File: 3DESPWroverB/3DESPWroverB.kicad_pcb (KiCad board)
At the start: 2 copper layers, 40 x 40 mm, 18 parts, among them J1 Conn_02x07_Odd_Even, J10 Conn_02x03_Odd_Even, J11 Conn_01x01, J12 Conn_01x01, J13 Conn_01x01, J14 Conn_01x01, J15 Conn_01x01, J16 Conn_01x01, J17 Conn_01x01, J18 Conn_01x01, J2 Conn_01x01, J3 Conn_01x01, J4 Conn_01x01, J5 Conn_01x01, J6 Conn_01x01, J7 Conn_01x01, J8 Conn_01x01, J9 Conn_01x01

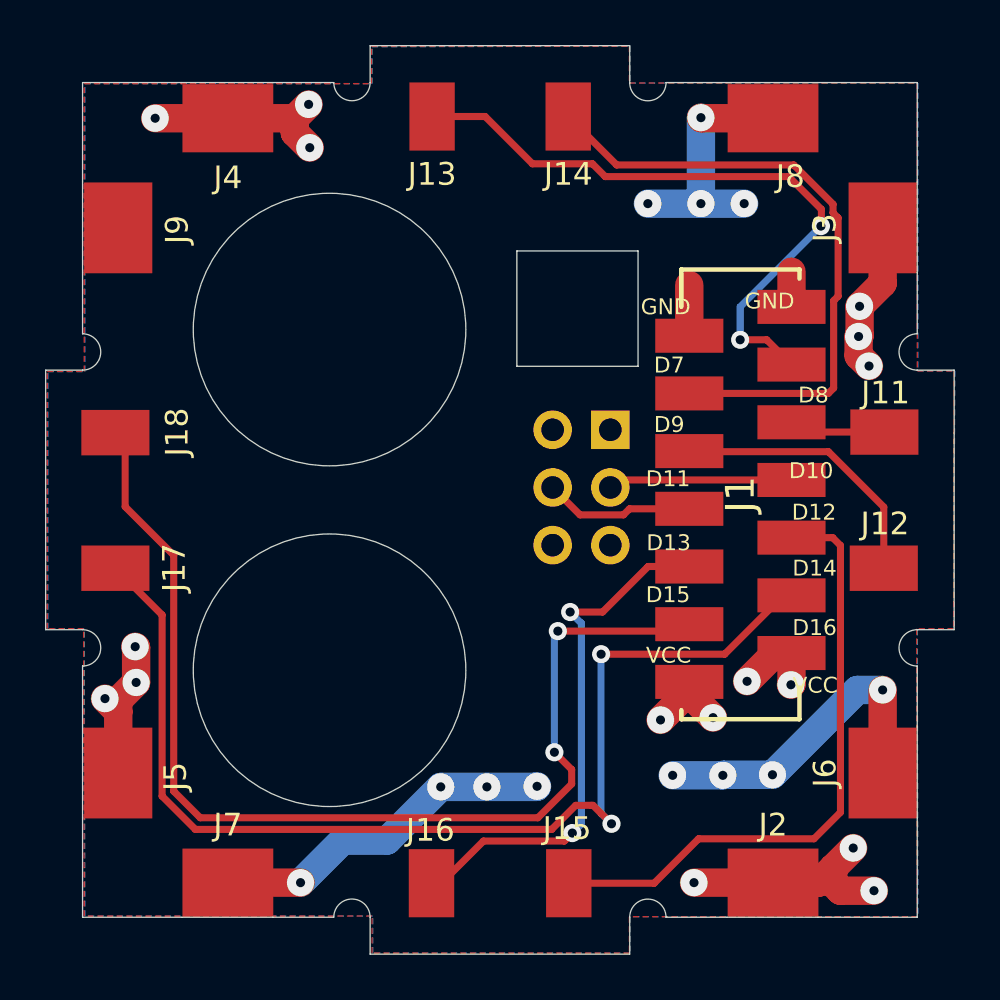
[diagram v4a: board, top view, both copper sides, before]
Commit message: Added 0805 diode before 3.3 power source
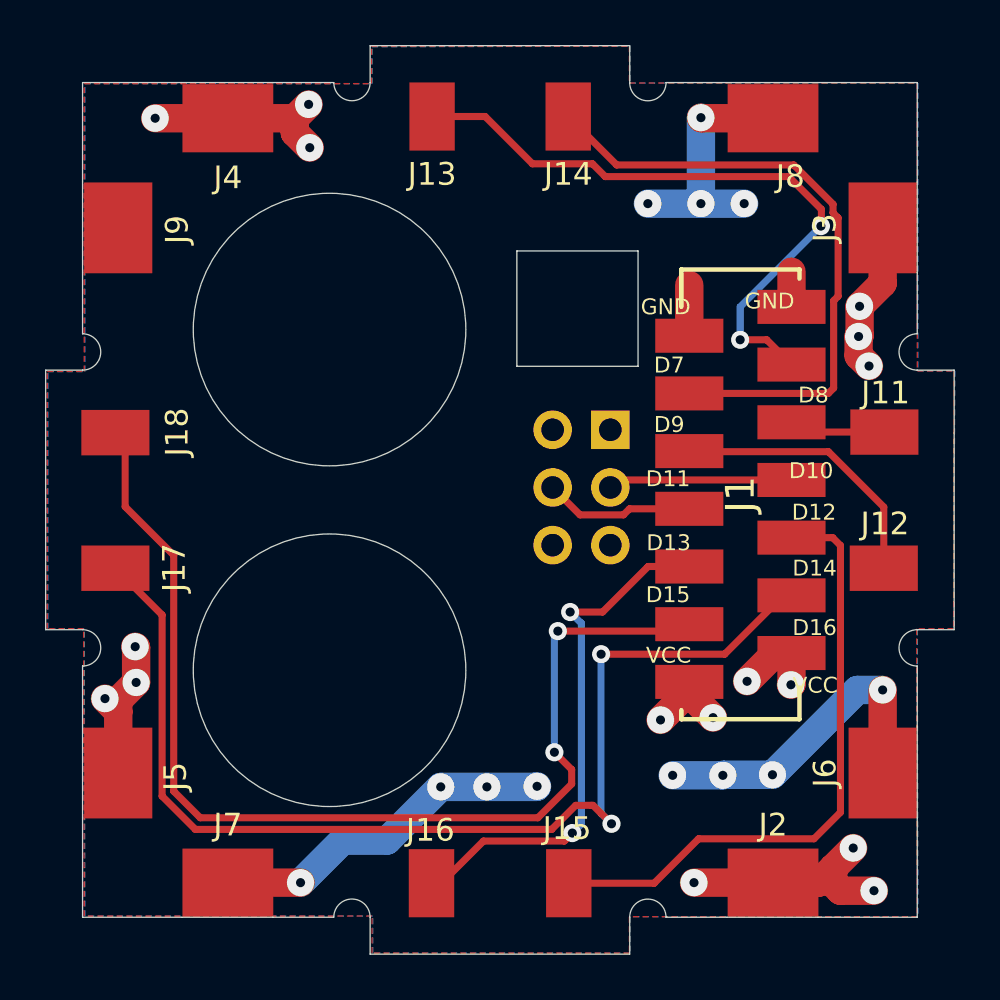
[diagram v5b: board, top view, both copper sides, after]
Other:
- net class Default removed
- net class Power removed
